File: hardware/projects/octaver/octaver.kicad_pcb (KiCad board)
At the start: 2 copper layers, 119.1 x 83.8 mm, 53 parts, among them J1 In, J2 Out, J3 Power, J4 pot_hp, J5 sw_hp, J6 fs_hp, J7 sw_hp2, SW1 Integrator On, SW2 stable / alive, SW3 Differentiator On, SW4 Octave Lo/Hi, SW6 Footswitch, U1 TL072, U2 TL072, U3 TL072, U5 LM311, U6 40175, U7 AD633JNZ

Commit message: update octaver/ with new library names
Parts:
- J1, J2: footprint circuits:mono_jack -> custom:mono_jack
- RV2, RV3, RV5, RV6, RV7, RV8: footprint circuits:Taiss_Potentiometer_vertical -> custom:Taiss_Potentiometer_vertical
- SW1, SW2, SW3, SW4: footprint circuits:Adam Tech SW-T3-2B-A-A3-S1 -> custom:Adam Tech SW-T3-2B-A-A3-S1
- SW6: footprint circuits:PBS-24-302_3PDT -> custom:PBS-24-302_3PDT
- U7: footprint footprints:N_8_ADI -> Package_DIP:DIP-8_W7.62mm

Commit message: make some edits & add some comments
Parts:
- added B1: MouseBite, Panelization:MouseBite-Slot_2.54x2.54mm_on-edge_D0.5mm_P0.85mm_4h_Trace, F.Cu at (96.5, 81.3)
- added B2: MouseBite, Panelization:MouseBite-Slot_2.54x2.54mm_on-edge_D0.5mm_P0.85mm_4h_Trace, F.Cu at (96.5, 33.0)
- added B3: MouseBite, Panelization:MouseBite-Slot_2.54x2.54mm_on-edge_D0.5mm_P0.85mm_4h_Trace, F.Cu at (66.0, 86.4)
- moved C5 4.30 mm to (152.4, 71.9)
- moved C6 4.30 mm to (150.9, 74.9)
- moved R10 4.30 mm to (152.4, 73.4)
- moved R11 4.30 mm to (120.9, 85.3)
- moved R13 4.30 mm to (151.1, 76.5)
- moved R20 4.30 mm to (139.7, 83.1)
- moved R8 4.30 mm to (137.1, 90.2)
- moved C3 4.30 mm to (133.3, 31.1)
- moved C9 4.30 mm to (114.3, 63.2)
- moved J3 4.30 mm to (127.0, 24.7)
- moved C1 4.30 mm to (150.5, 92.2)
- moved C2 4.30 mm to (134.6, 75.7)
- moved J7 4.30 mm to (149.5, 97.0)
- moved R9 4.30 mm to (137.1, 92.7)
- moved SW2 4.30 mm to (132.9, 88.5)
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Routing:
- net GNDPWR: track 185.7 -> 182.4 mm
- net GND: vias 9 -> 34
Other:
- board size 119.1 x 83.8 mm -> 121 x 84.5 mm
- board text added: "CR(nausicaa): added more via pinning up here, as well as in some locations lower down to improve flow in GND."
- board text added: "CR(nausicaa): there are some silkscreen cutoffs. up to you where you want to move the text (if at all)."
- board text added: "CR(nausicaa): used L to toggle locking for all the stuff that's position-sensitive. forgot that was a thing, but it's the fastest way of keeping things from moving."
- board text added: "CR(nausicaa): we might consider changing the pour net on this board to GNDPWR instead of GND, so we can star-ground the audio reference. except that GNDPWR has to be the same DC level as the input..."

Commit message: make final (?) major edits
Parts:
- B1, B2, B3: footprint Panelization:MouseBite-Slot_2.54x2.54mm_on-edge_D0.5mm_P0.85mm_4h_Trace -> custom:MouseBite_2.54x7.62mm_JLCPCB
- D1: moved to B.Cu
- moved R6 32.8 mm to (112.5, 45.1)
- moved C3 32.2 mm to (107.4, 50.2)
- moved C4 32.2 mm to (117.1, 50.3)
- moved R7 32.1 mm to (112.5, 55.9)
- moved J3 21.2 mm to (129.5, 45.7), turned to 90 degrees
- moved B2 19.1 mm to (95.2, 52.1)
- moved B1 14.0 mm to (95.2, 95.2)
- moved U7 13.2 mm to (152.4, 45.7)
- moved B3 2.29 mm to (67.9, 85.1)
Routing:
- net Net-(J5B-Pin_2): track 80.2 -> 93.4 mm
- net Net-(J5H-Pin_3): track 46.6 -> 58.4 mm
- net Net-(SW3-C): track 34.3 -> 46.0 mm
- net +9V: track 174.2 -> 179.8 mm, vias 7 -> 9
- net GNDPWR: track 182.4 -> 184.1 mm
- net GND: vias 34 -> 31
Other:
- outline, holes or cut-outs redrawn
- board text removed: "CR(nausicaa): added more via pinning up here, as well as in some locations lower down to improve flow in GND."
- board text removed: "CR(nausicaa): there are some silkscreen cutoffs. up to you where you want to move the text (if at all)."
- board text removed: "CR(nausicaa): used L to toggle locking for all the stuff that's position-sensitive. forgot that was a thing, but it's the fastest way of keeping things from moving."
- board text removed: "CR(nausicaa): we might consider changing the pour net on this board to GNDPWR instead of GND, so we can star-ground the audio reference. except that GNDPWR has to be the same DC level as the input..."

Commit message: prep for JLC order
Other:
- board text added: "JLCJLCJLCJLC"
- board text added: "all-in-one crushed tomatoes vine-ripened tomatoes not from concentrate chunky ;)"
- board text added: "footswitch board"
- board text added: "i love spaghetti (?)"
- board text added: "let the calculus flow through you"
- board text added: "main board"
- board text added: "pot board"
- board text added: "the can v0.1 © 2026 stillmar electric <3 aspen, chris, & nausicaa"
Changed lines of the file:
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@@
 		(sheetname "/")
 		(sheetfile "octaver.kicad_sch")
-		(attr exclude_from_bom)
+		(attr exclude_from_pos_files exclude_from_bom)
 		(duplicate_pad_numbers_are_jumpers no)
 		(fp_line
@@
 		(sheetname "/")
 		(sheetfile "octaver.kicad_sch")
-		(attr through_hole)
+		(attr through_hole exclude_from_pos_files exclude_from_bom)
 		(duplicate_pad_numbers_are_jumpers no)
 		(fp_line
@@
 		(sheetname "/")
 		(sheetfile "octaver.kicad_sch")
-		(attr through_hole)
+		(attr through_hole exclude_from_pos_files exclude_from_bom)
 		(duplicate_pad_numbers_are_jumpers no)
 		(fp_line
@@
 		(sheetname "/")
 		(sheetfile "octaver.kicad_sch")
-		(attr through_hole)
+		(attr through_hole exclude_from_pos_files exclude_from_bom)
 		(duplicate_pad_numbers_are_jumpers no)
 		(fp_line
@@
 		(sheetname "/")
 		(sheetfile "octaver.kicad_sch")
-		(attr exclude_from_bom)
+		(attr exclude_from_pos_files exclude_from_bom)
 		(duplicate_pad_numbers_are_jumpers no)
 		(fp_line
@@
 		(sheetname "/")
 		(sheetfile "octaver.kicad_sch")
-		(attr through_hole)
+		(attr through_hole exclude_from_pos_files exclude_from_bom)
 		(duplicate_pad_numbers_are_jumpers no)
 		(fp_line
@@
 		(sheetname "/")
 		(sheetfile "octaver.kicad_sch")
-		(attr through_hole)
+		(attr through_hole exclude_from_pos_files exclude_from_bom)
 		(duplicate_pad_numbers_are_jumpers no)
 		(fp_line
@@
 		(sheetname "/")
 		(sheetfile "octaver.kicad_sch")
-		(attr through_hole)
+		(attr through_hole exclude_from_pos_files exclude_from_bom)
 		(duplicate_pad_numbers_are_jumpers no)
 		(fp_line
@@
 		(sheetname "/")
 		(sheetfile "octaver.kicad_sch")
-		(attr exclude_from_bom)
+		(attr exclude_from_pos_files exclude_from_bom)
 		(duplicate_pad_numbers_are_jumpers no)
 		(fp_line
@@
 		(sheetname "/")
 		(sheetfile "octaver.kicad_sch")
-		(attr through_hole)
+		(attr through_hole exclude_from_pos_files exclude_from_bom)
 		(duplicate_pad_numbers_are_jumpers no)
 		(fp_line
@@
 		(sheetname "/")
 		(sheetfile "octaver.kicad_sch")
-		(attr through_hole)
+		(attr through_hole exclude_from_pos_files exclude_from_bom)
 		(duplicate_pad_numbers_are_jumpers no)
 		(fp_line
@@
 		(sheetname "/")
 		(sheetfile "octaver.kicad_sch")
-		(attr through_hole)
+		(attr through_hole exclude_from_pos_files exclude_from_bom)
 		(duplicate_pad_numbers_are_jumpers no)
 		(fp_line
@@
 		(sheetname "/")
 		(sheetfile "octaver.kicad_sch")
-		(attr through_hole)
+		(attr through_hole exclude_from_pos_files exclude_from_bom)
 		(duplicate_pad_numbers_are_jumpers no)
 		(fp_line
@@
 		(sheetname "/")
 		(sheetfile "octaver.kicad_sch")
-		(attr through_hole)
+		(attr through_hole exclude_from_pos_files exclude_from_bom)
 		(duplicate_pad_numbers_are_jumpers no)
 		(fp_line
@@
 		(sheetname "/")
 		(sheetfile "octaver.kicad_sch")
-		(attr through_hole)
+		(attr through_hole exclude_from_pos_files exclude_from_bom)
 		(duplicate_pad_numbers_are_jumpers no)
 		(fp_line
@@
 		(sheetname "/")
 		(sheetfile "octaver.kicad_sch")
-		(attr through_hole)
+		(attr through_hole exclude_from_pos_files exclude_from_bom)
 		(duplicate_pad_numbers_are_jumpers no)
 		(fp_line
@@
 		(sheetname "/")
 		(sheetfile "octaver.kicad_sch")
-		(attr through_hole)
+		(attr through_hole exclude_from_pos_files exclude_from_bom)
 		(duplicate_pad_numbers_are_jumpers no)
 		(fp_rect
@@
 		(sheetname "/")
 		(sheetfile "octaver.kicad_sch")
-		(attr through_hole)
+		(attr through_hole exclude_from_pos_files exclude_from_bom)
 		(duplicate_pad_numbers_are_jumpers no)
 		(fp_line
@@
 		(sheetname "/")
 		(sheetfile "octaver.kicad_sch")
-		(attr through_hole)
+		(attr through_hole exclude_from_pos_files exclude_from_bom)
 		(duplicate_pad_numbers_are_jumpers no)
 		(fp_rect
@@
 		(sheetname "/")
 		(sheetfile "octaver.kicad_sch")
-		(attr through_hole)
+		(attr through_hole exclude_from_pos_files exclude_from_bom)
 		(duplicate_pad_numbers_are_jumpers no)
 		(fp_rect
@@
 		(sheetname "/")
 		(sheetfile "octaver.kicad_sch")
-		(attr through_hole)
+		(attr through_hole exclude_from_pos_files exclude_from_bom)
 		(duplicate_pad_numbers_are_jumpers no)
 		(fp_rect
@@
 		(sheetname "/")
 		(sheetfile "octaver.kicad_sch")
-		(attr through_hole)
+		(attr through_hole exclude_from_pos_files exclude_from_bom)
 		(duplicate_pad_numbers_are_jumpers no)
 		(fp_rect
@@
 		(sheetname "/")
 		(sheetfile "octaver.kicad_sch")
-		(attr through_hole)
+		(attr through_hole exclude_from_pos_files exclude_from_bom)
 		(duplicate_pad_numbers_are_jumpers no)
 		(fp_line
@@
 		(sheetname "/")
 		(sheetfile "octaver.kicad_sch")
-		(attr through_hole)
+		(attr through_hole exclude_from_pos_files exclude_from_bom)
 		(duplicate_pad_numbers_are_jumpers no)
 		(fp_line
@@
 		(layer "Edge.Cuts")
 	)
+	(gr_text "let the calculus flow through you"
+		(at 36.068 88.392 0)
+		(layer "F.SilkS")
+		(effects
+			(font
+				(size 0.5 0.5)
+				(thickness 0.08)
+			)
+			(justify left bottom)
+		)
+	)
+	(gr_text "the can v0.1\n© 2026 stillmar electric\n<3 aspen, chris, & nausicaa"
+		(at 42.545 25.4 0)
+		(layer "F.SilkS")
+		(effects
+			(font
+				(size 0.5 0.5)
+				(thickness 0.08)
+			)
+			(justify left bottom)
+		)
+	)
+	(gr_text "JLCJLCJLCJLC"
+		(at 45.72 105.41 0)
+		(layer "F.SilkS")
+		(effects
+			(font
+				(size 0.5 0.5)
+				(thickness 0.08)
+			)
+			(justify left bottom)
+		)
+	)
+	(gr_text "the can v0.1\n© 2026 stillmar electric\n<3 aspen, chris, & nausicaa"
+		(at 75.565 106.045 0)
+		(layer "F.SilkS")
+		(effects
+			(font
+				(size 0.5 0.5)
+				(thickness 0.08)
+			)
+			(justify left bottom)
+		)
+	)
+	(gr_text "the can v0.1\n© 2026 stillmar electric\n<3 aspen, chris, & nausicaa"
+		(at 97.79 98.425 0)
+		(layer "F.SilkS")
+		(effects
+			(font
+				(size 0.5 0.5)
+				(thickness 0.08)
+			)
+			(justify left bottom)
+		)
+	)
+	(gr_text "footswitch board"
+		(at 36.195 90.805 0)
+		(layer "F.SilkS")
+		(effects
+			(font
+				(size 1 1)
+				(thickness 0.1)
+			)
+			(justify left bottom)
+		)
+	)
+	(gr_text "pot board"
+		(at 78.74 24.13 0)
+		(layer "F.SilkS")
+		(effects
+			(font
+				(size 1 1)
+				(thickness 0.1)
+			)
+			(justify left bottom)
+		)
+	)
+	(gr_text "main board"
+		(at 145.415 42.545 0)
+		(layer "F.SilkS")
+		(effects
+			(font
+				(size 1 1)
+				(thickness 0.1)
+			)
+			(justify left bottom)
+		)
+	)
+	(gr_text "i love spaghetti (?)"
+		(at 98.552 71.12 75)
+		(layer "F.SilkS")
+		(effects
+			(font
+				(size 1 1)
+				(thickness 0.15)
+			)
+			(justify left bottom)
+		)
+	)
 	(gr_text "+"
 		(locked yes)
@@
 		)
 	)
+	(gr_text "all-in-one crushed tomatoes\n  vine-ripened tomatoes\n    not from concentrate\n      chunky ;)"
+		(at 53.848 53.848 -75)
+		(layer "B.SilkS")
+		(effects
+			(font
+				(size 0.6 0.6)
+				(thickness 0.1)
+			)
+			(justify left bottom mirror)
+		)
+	)

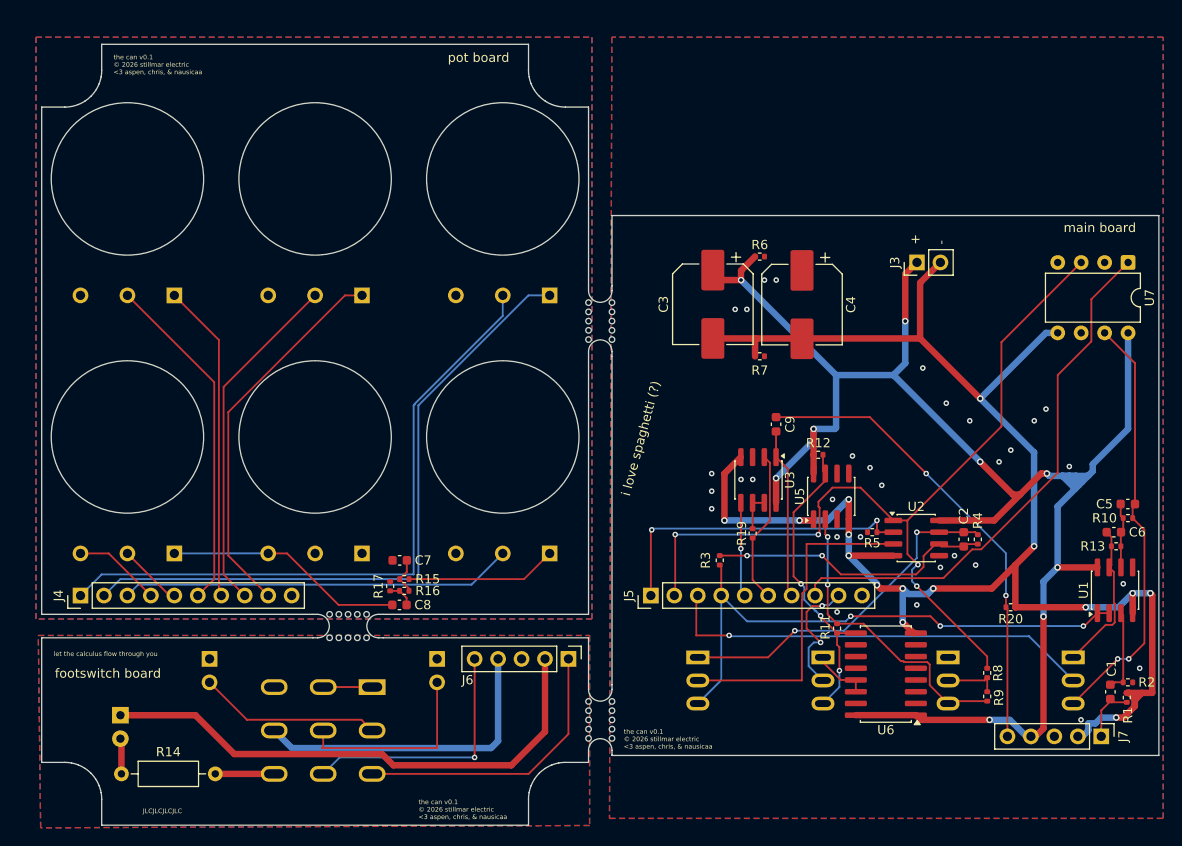
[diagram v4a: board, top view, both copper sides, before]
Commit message: octaver: Most of the rev2 fixes
Most notably, fixed the whine by switching pre-gain to an inverting amp
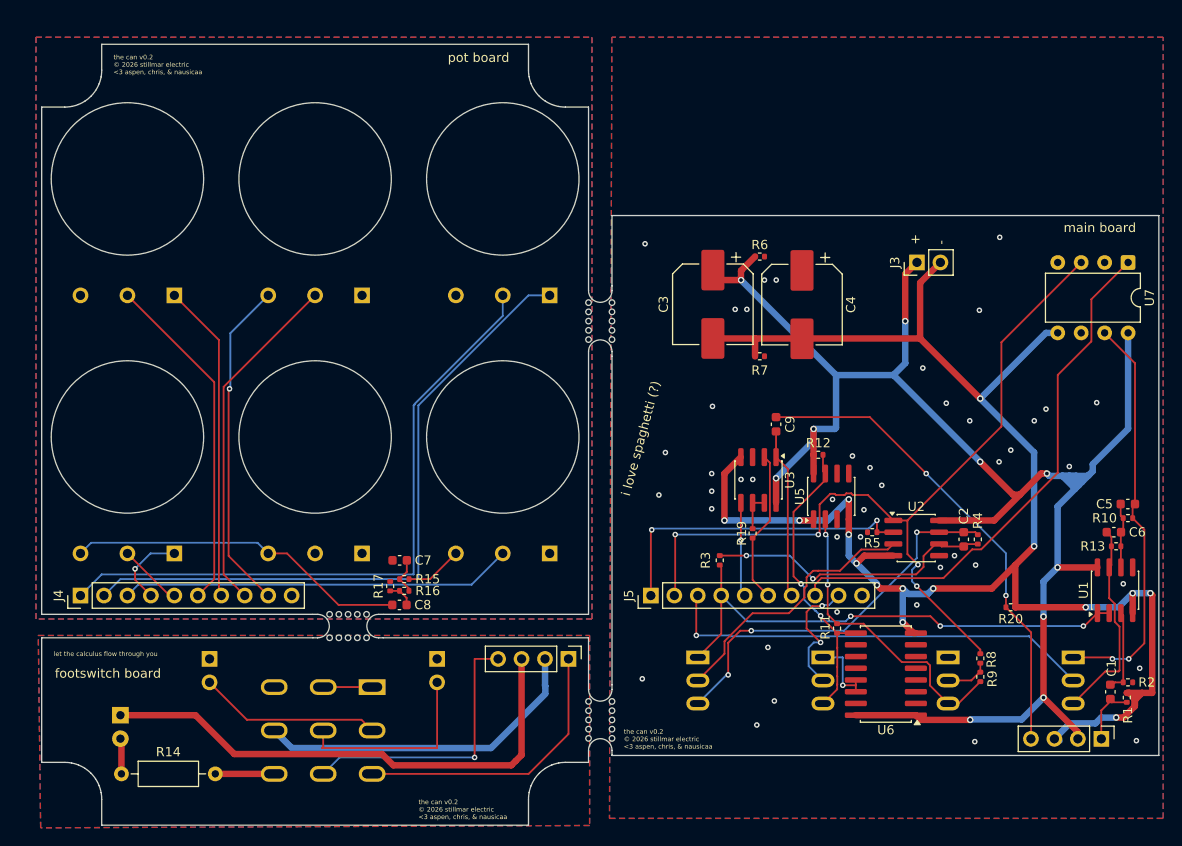
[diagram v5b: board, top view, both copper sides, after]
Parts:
- removed J6: fs_hp, Connector_PinHeader_2.54mm:PinHeader_1x05_P2.54mm_Vertical
- removed J7: sw_hp2, Connector_PinHeader_2.54mm:PinHeader_1x05_P2.54mm_Vertical
- added J8: main board, Connector_PinHeader_2.54mm:PinHeader_1x04_P2.54mm_Vertical, F.Cu at (149.5, 97.3)
- added J9: fs board, Connector_PinHeader_2.54mm:PinHeader_1x04_P2.54mm_Vertical, F.Cu at (91.8, 88.6)
- RV5: value A100K -> C100K
- RV8: value A1M -> C1M
- moved R9 2.24 mm to (136.4, 90.6)
- moved R8 1.74 mm to (136.4, 88.6)
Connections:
- net Net-(SW2-C) renamed /live
- net Net-(SW4-A) renamed /octave_lo
- net Net-(SW4-C) renamed /octave_hi
- C2 pad 1: Net-(SW1-A) -> /int_on
- C5 pad 2: Net-(SW3-C) -> /diff bypass
- C6 pad 1: Net-(SW3-A) -> /diff on
- D1 pad 1: Net-(D1-K) -> fs_gndpwr
- J1 pad S: /fsgnd -> fs_gndpwr
- J2 pad S: /fsgnd -> fs_gndpwr
- J5 pad 4: Net-(J5D-Pin_3) -> /int_off
- R10 pad 2: Net-(SW3-C) -> /diff bypass
- R13 pad 1: Net-(SW3-A) -> /diff on
- R3 pad 2: Net-(J5D-Pin_3) -> /int_off
- R4 pad 1: Net-(SW1-A) -> /int_on
- RV2 pad 1: Net-(J4I-Pin_3) -> pot_gnd
- RV2 pad 3: pot_gnd -> Net-(J4I-Pin_3)
- RV3 pad 1: Net-(C8-Pad2) -> Net-(J4D-Pin_3)
- RV3 pad 3: Net-(J4D-Pin_3) -> Net-(C8-Pad2)
- RV5 pad 1: Net-(R15-Pad2) -> unconnected-(RV5-Pad1)
- RV5 pad 3: unconnected-(RV5-Pad3) -> Net-(R15-Pad2)
- SW1 pad 1: Net-(SW1-A) -> /int_off
- SW1 pad 3: Net-(J5D-Pin_3) -> /int_on
- SW2 pad 1: unconnected-(SW2-A-Pad1) -> /stable
- SW3 pad 1: Net-(SW3-A) -> /diff bypass
- SW3 pad 3: Net-(SW3-C) -> /diff on
- SW6 pad 3: Net-(J6A-Pin_3) -> fs_in
- SW6 pad 6: Net-(J6E-Pin_3) -> fs_out
- SW6 pad 8: Net-(J6D-Pin_3) -> fs_pwr
- U1 pad 1: Net-(J5D-Pin_3) -> /int_off
- U1 pad 2: Net-(J5D-Pin_3) -> /int_off
- U1 pad 7: Net-(SW3-A) -> /diff on
- U2 pad 7: Net-(SW1-A) -> /int_on
- U7 pad 7: Net-(SW3-C) -> /diff bypass
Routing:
- net Net-(J5D-Pin_3): track 60.5 -> 0.00 mm, vias 3 -> 0
- net Net-(D1-K): track 57.6 -> 0.00 mm
- net fs_gndpwr: track 0.00 -> 56.6 mm
- net /int_off: track 0.00 -> 55.5 mm, vias 0 -> 3
- net Net-(SW3-C): track 46.0 -> 0.00 mm, vias 2 -> 0
- net /diff bypass: track 0.00 -> 44.1 mm, vias 0 -> 2
- net /int_on: track 0.00 -> 41.8 mm, vias 0 -> 3
- net Net-(SW1-A): track 37.7 -> 0.00 mm, vias 2 -> 0
- net fs_pwr: track 0.00 -> 36.4 mm
- net Net-(J6D-Pin_3): track 34.2 -> 0.00 mm
- net fs_in: track 0.00 -> 31.2 mm
- net Net-(J6A-Pin_3): track 31.2 -> 0.00 mm
- net fs_out: track 0.00 -> 30.3 mm, vias 0 -> 1
- net Net-(J6E-Pin_3): track 27.8 -> 0.00 mm, vias 1 -> 0
- net /diff on: track 0.00 -> 22.3 mm
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- added copper zone on B.Cu, net fs_gndpwr
- added copper zone on F.Cu, net fs_gndpwr
- removed copper zone on B.Cu, net /fsgnd
- removed copper zone on F.Cu, net /fsgnd
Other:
- board text added: "the can v0.2 © 2026 stillmar electric <3 aspen, chris, & nausicaa"
- board text removed: "JLCJLCJLCJLC"
- board text removed: "the can v0.1 © 2026 stillmar electric <3 aspen, chris, & nausicaa"
